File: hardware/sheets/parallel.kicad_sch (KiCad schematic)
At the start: 20 parts, among them J1 DB25_Pins, U1 74HCT574, U10 74HCT32, U11 74HCT32, U12 74HCT00, U13 74HCT125, U2 74HCT574, U3 74HCT244, U4 74HCT245, U5 74HCT244, U6 74HCT138, U7 74HCT08, U8 74HCT08, U9 74HCT04

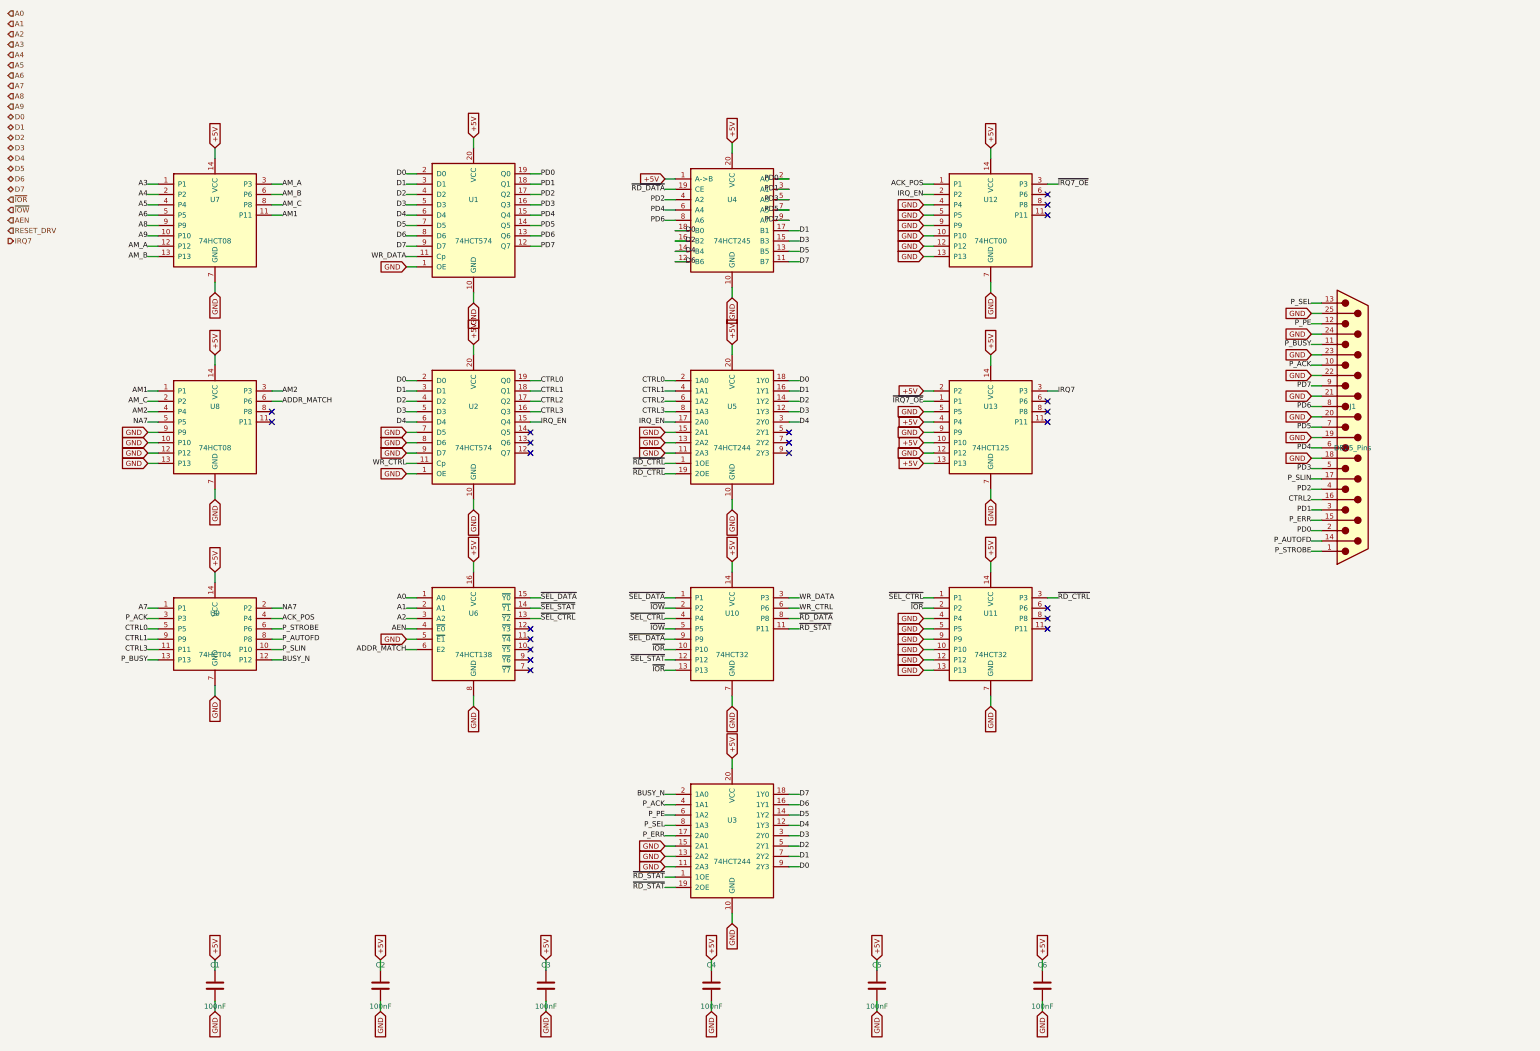
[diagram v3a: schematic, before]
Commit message: Design review 2026-07-11: rail protection, decoupling, wiring fixes
Protection:
- Sidecar +5V now feeds through a 2A polyfuse into +5V_ISA with an
  SMBJ5.0A clamp + 22uF bulk (a faulted ISA card trips its own fuse
  instead of dropping the board; back-fed voltage is clamped).
- USB-C VBUS enters through a 3A polyfuse with an SMBJ5.0A on +5V
  (backstop for the CFG1 9-20V failure mode). CH224K gains a 1uF VDD
  cap; its PG routes to Supervisor GPIO16 as PD_PG. Buck output
  doubled to 2x22uF, 10uF at VIN, extra rail bulk.
- Supervisor USB-A host port: 27R series termination (RP2040
  requirement), USBLC6-2SC6 ESD array, 100uF VBUS bulk.
- Video: HDMI +5V fused (500mA), HPD sensed on GPIO41, 100R series on
  VGA sync. TMDS ESD array deferred to layout (no symbol).
- card_isatest: V5RAW bulk, Q1 gate soft-start cap, TVS on DUT rail.

Wiring fixes:
- SPKR had no driver anywhere (netlist: 1 node). Bus MCU GPIO22
  reassigned from the diagnostics-only bus-CLK sense to SPKR; bus_mcu
  drops CLK from its interface. Doc 5.2 updated.
- bus_mcu C8 decoupled +3V3, a rail that sheet never uses -> 3V3_BUS.
- Storage IRQ5 was push-pull (permanently driven when idle) -> 2N7002
  + gated '125 tri-state, same convention as the LPT IRQ7 stage.
- MAX3241 pump caps resized to the 5V datasheet values (47nF/330nF).
- LPT DB25 status inputs get 4.7k pull-ups (floated with no printer).
- Audio line-out gets a 100R series isolator before the jack.

Best practices:
- Decoupling to ~1x100nF per IC on every sheet + bulk per board
  (cpu_core 7->16 incl. the naked 3.3V oscillator, storage 4->11,
  parallel 6->13, rtc/com/video/bus_mcu/card_isatest similar).
- All floating spare CMOS inputs tied ('00/'74/'157/'02/'04/'125
  sections across cpu_core, bus_mcu, rtc, storage, card_isatest).

Sourcing: new parts mapped in parts.py with JLC-verified LCSC numbers;
Power_Protection lib registered in the tools; TPS563200 stock alert
(4 pcs left at JLC) flagged in parts.py + jlcpcb-sourcing.md. All
decisi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
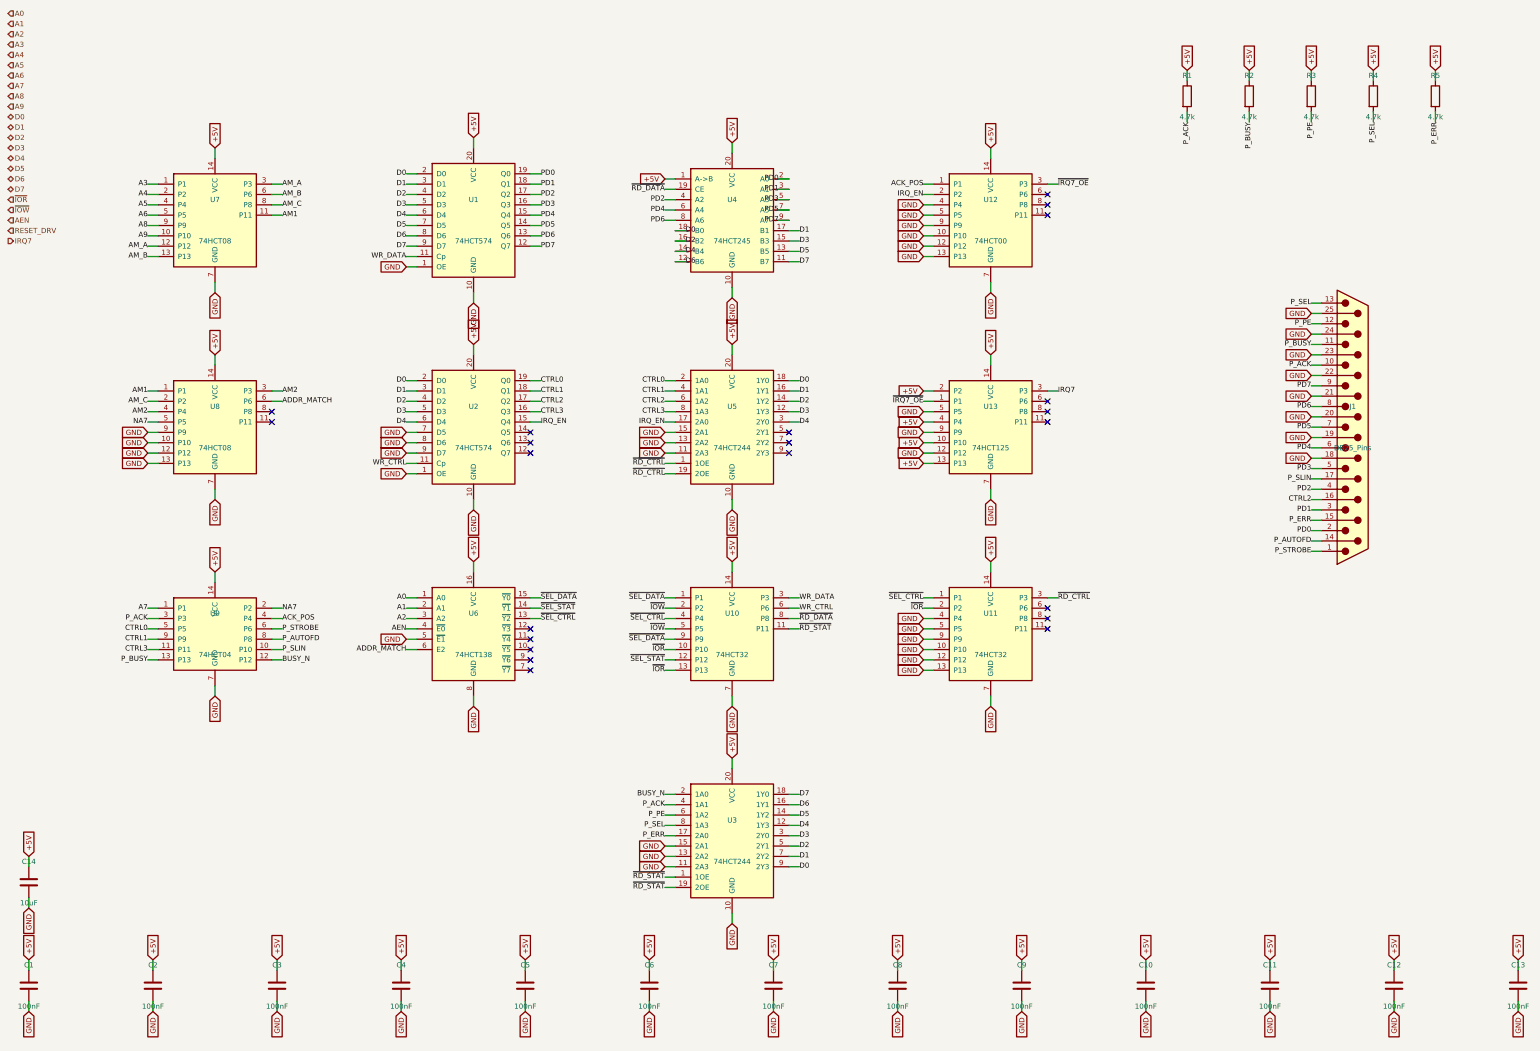
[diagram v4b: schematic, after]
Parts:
- added C10, C11, C12, C13, C2, C3, C4, C5, C6, C7, C8, C9: 100nF, symbol Device:C
- added C14: 10uF, symbol Device:C
- R1: renamed from C1; value 100nF -> 4.7k; symbol Device:C -> Device:R; LCSC Part Num C14663 -> C23162
- R2: renamed from C2; value 100nF -> 4.7k; symbol Device:C -> Device:R; LCSC Part Num C14663 -> C23162
- R3: renamed from C3; value 100nF -> 4.7k; symbol Device:C -> Device:R; LCSC Part Num C14663 -> C23162
- R4: renamed from C4; value 100nF -> 4.7k; symbol Device:C -> Device:R; LCSC Part Num C14663 -> C23162
- R5: renamed from C5; value 100nF -> 4.7k; symbol Device:C -> Device:R; LCSC Part Num C14663 -> C23162
- renumbered C6 to C1
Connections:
- net +5V: now also C10.1, C11.1, C12.1, C13.1, C14.1, C2.1, C3.1, C4.1, C5.1, C6.1, C7.1, C8.1, C9.1
- net GND: now also C10.2, C11.2, C12.2, C13.2, C14.2, C2.2, C3.2, C4.2, C5.2, C6.2, C7.2, C8.2, C9.2; no longer R1.2, R2.2, R3.2, R4.2, R5.2
- net P_ACK: now also R1.2
- net P_BUSY: now also R2.2
- net P_ERR: now also R5.2
- net P_PE: now also R3.2
- net P_SEL: now also R4.2
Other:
- moved on the sheet: C1

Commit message: COM/LPT: on-board enable jumpers + base-addr/IRQ straps
The motherboard's COM1/COM2 IRQs were hard-wired at build time (INSTANCES
net remap); the LPT port had no strap or disable at all. Both sheets now
carry the full jumper set a real card would have, so an on-board port can
be disabled or re-strapped to make room for the same peripheral on the
sidecar chain:

- com_port: JP3 enable gates the 16550's spare active-high CS1 (open =
  never selected; IRQ needs no gating since MCR resets to 0 -> OUT2# high
  -> '125 released). JP2 picks IRQ4/IRQ3 (open = polled) on the sheet, so
  the sheet now exports IRQ3+IRQ4 and the INSTANCES remap is gone -- both
  instances share the lines safely (tri-state). J2 base strap unchanged.
- parallel: JP1 base 0x378/0x278 (differ only in A8; a spare U12 NAND
  makes ~A8), JP2 enable lifts the register-select '138's spare ~E1 (open
  kills every select, read enable and latch clock), JP3 IRQ7/IRQ5 (open =
  polled; IRQ5 noted as conflicting with the storage card if both enabled).
  PINS now export IRQ5+IRQ7.
- parts.py: Conn_01x02 breakaway-header fallback for the 2-pin jumpers.

Downstream sheet .kicad_sch diffs are instance-path UUID shifts from the
grown com_port/parallel interfaces (deterministic counter), not edits.

Verified: netlist shows IRQ3/IRQ4 spanning sidecar + both COM straps + the
Bus MCU collector; IRQ5 spans sidecar + LPT strap + storage + collector;
each enable net ties jumper + pull resistor + chip-select pin. Zero
structural ERC on motherboard and cards.

Co-Authored-By: Claude Fable 5 <noreply@anthropic.com>
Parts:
- added JP1: BASE 378/278, symbol Connector_Generic:Conn_01x03
- added JP2: LPT_EN, symbol Connector_Generic:Conn_01x02
- added JP3: IRQ strap, symbol Connector_Generic:Conn_01x03
- added R6: 10k, symbol Device:R
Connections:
- net +5V: now also R6.1
- net A8: now also U12.4 (P4), U12.5 (P5), JP1.1 (Pin_1); no longer U7.9 (P9)
- net GND: now also JP2.2 (Pin_2); no longer U12.4 (P4), U12.5 (P5), U6.5 (~{E1})
- net IRQ7: now also JP3.1 (Pin_1); no longer U13.3 (P3)
- net NA8: now reaches U12.6 (P6)
- net NA8: now also JP1.3 (Pin_3)
- new net A8_SEL: JP1.2 (Pin_2), U7.9 (P9)
- new net IRQ5: JP3.3 (Pin_3)
- new net LPT_IRQ: JP3.2 (Pin_2), U13.3 (P3)
- new net ~{LPT_EN}: JP2.1 (Pin_1), R6.2, U6.5 (~{E1})
- no-connect marks 22 -> 21
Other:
- note added: "JP1: base 0x378/0x278; JP2: open=port disabled; JP3: IRQ7/IRQ5/open=polled"
